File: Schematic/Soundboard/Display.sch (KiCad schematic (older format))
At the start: 2 parts, among them J5 Conn_01x40_MountingPin

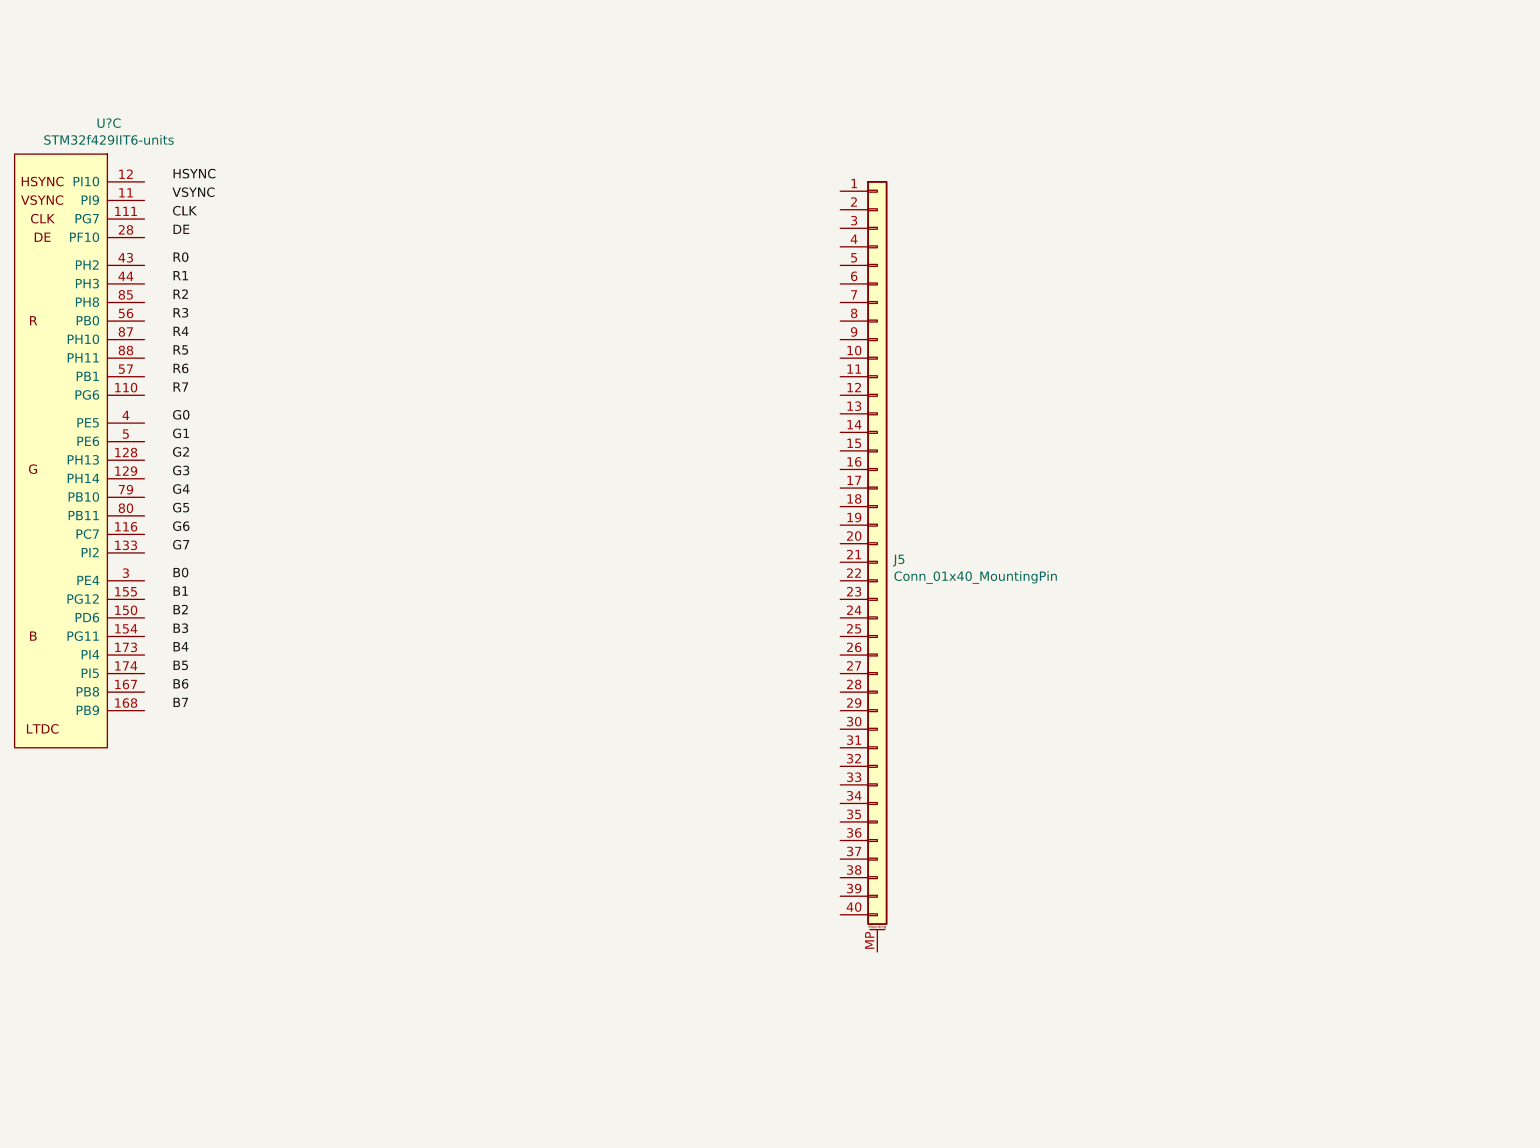
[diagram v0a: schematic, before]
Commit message: Complete part selection. Start connections
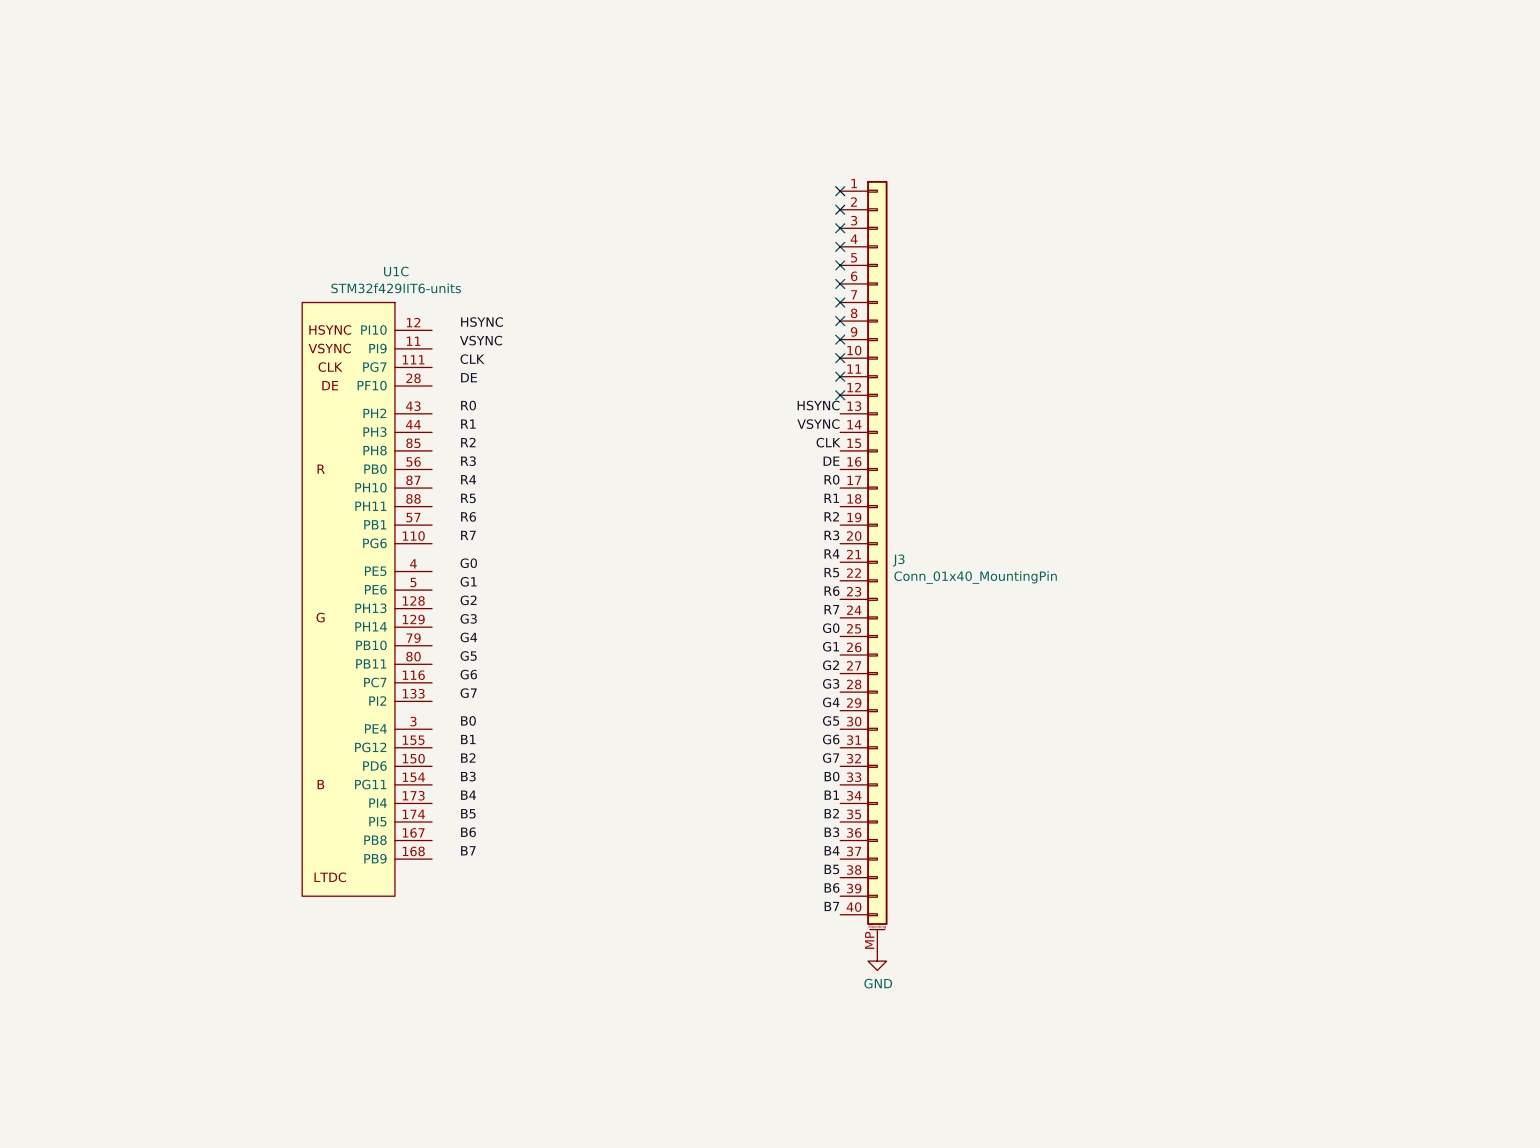
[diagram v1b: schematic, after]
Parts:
- removed U?: STM32f429IIT6-units, symbol Soundboard:STM32f429IIT6-units
- added U1: STM32f429IIT6-units, symbol Soundboard:STM32f429IIT6-units
- renumbered J5 to J3
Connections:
- net B0: now also J3.33 (Pin_33)
- net B1: now also J3.34 (Pin_34)
- net B2: now also J3.35 (Pin_35)
- net B3: now also J3.36 (Pin_36)
- net B4: now also J3.37 (Pin_37)
- net B5: now also J3.38 (Pin_38)
- net B6: now also J3.39 (Pin_39)
- net B7: now also J3.40 (Pin_40)
- net CLK: now also J3.15 (Pin_15)
- net DE: now also J3.16 (Pin_16)
- net G0: now also J3.25 (Pin_25)
- net G1: now also J3.26 (Pin_26)
- net G2: now also J3.27 (Pin_27)
- net G3: now also J3.28 (Pin_28)
- net G4: now also J3.29 (Pin_29)
- net G5: now also J3.30 (Pin_30)
- net G6: now also J3.31 (Pin_31)
- net G7: now also J3.32 (Pin_32)
- net HSYNC: now also J3.13 (Pin_13)
- net R0: now also J3.17 (Pin_17)
- net R1: now also J3.18 (Pin_18)
- net R2: now also J3.19 (Pin_19)
- net R3: now also J3.20 (Pin_20)
- net R4: now also J3.21 (Pin_21)
- net R5: now also J3.22 (Pin_22)
- net R6: now also J3.23 (Pin_23)
- net R7: now also J3.24 (Pin_24)
- net VSYNC: now also J3.14 (Pin_14)
- net GND: now reaches J3.MP (MountPin)
- no-connect marks 0 -> 12
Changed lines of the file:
@@
 EESchema Schematic File Version 4
-EELAYER 30 0
+LIBS:Soundboard-cache
+EELAYER 26 0
 EELAYER END
 $Descr A4 11693 8268
 encoding utf-8
-Sheet 6 6
+Sheet 5 7
 Title ""
 Date ""
@@
 Comment4 ""
 $EndDescr
-Text Label 3650 1800 0    50   ~ 0
+Text Label 5200 2600 0    50   ~ 0
 HSYNC
-Text Label 3650 1900 0    50   ~ 0
+Text Label 5200 2700 0    50   ~ 0
 VSYNC
-Text Label 3650 3800 0    50   ~ 0
+Text Label 5200 4600 0    50   ~ 0
 G7
-Text Label 3650 3700 0    50   ~ 0
+Text Label 5200 4500 0    50   ~ 0
 G6
-Text Label 3650 3600 0    50   ~ 0
+Text Label 5200 4400 0    50   ~ 0
 G5
-Text Label 3650 3100 0    50   ~ 0
+Text Label 5200 3900 0    50   ~ 0
 G0
-Text Label 3650 3200 0    50   ~ 0
+Text Label 5200 4000 0    50   ~ 0
 G1
-Text Label 3650 3500 0    50   ~ 0
+Text Label 5200 4300 0    50   ~ 0
 G4
-Text Label 3650 3400 0    50   ~ 0
+Text Label 5200 4200 0    50   ~ 0
 G3
-Text Label 3650 3300 0    50   ~ 0
+Text Label 5200 4100 0    50   ~ 0
 G2
-Text Label 3650 2650 0    50   ~ 0
+Text Label 5200 3450 0    50   ~ 0
 R4
-Text Label 3650 2450 0    50   ~ 0
+Text Label 5200 3250 0    50   ~ 0
 R2
-Text Label 3650 2350 0    50   ~ 0
+Text Label 5200 3150 0    50   ~ 0
 R1
-Text Label 3650 2250 0    50   ~ 0
+Text Label 5200 3050 0    50   ~ 0
 R0
-Text Label 3650 2000 0    50   ~ 0
+Text Label 5200 2800 0    50   ~ 0
 CLK
-Text Label 3650 2950 0    50   ~ 0
+Text Label 5200 3750 0    50   ~ 0
 R7
-Text Label 3650 2100 0    50   ~ 0
+Text Label 5200 2900 0    50   ~ 0
 DE
-Text Label 3650 2550 0    50   ~ 0
+Text Label 5200 3350 0    50   ~ 0
 R3
-Text Label 3650 2850 0    50   ~ 0
+Text Label 5200 3650 0    50   ~ 0
 R6
-Text Label 3650 2750 0    50   ~ 0
+Text Label 5200 3550 0    50   ~ 0
 R5
-Text Label 3650 4150 0    50   ~ 0
+Text Label 5200 4950 0    50   ~ 0
 B2
-Text Label 3650 4450 0    50   ~ 0
+Text Label 5200 5250 0    50   ~ 0
 B5
-Text Label 3650 4650 0    50   ~ 0
+Text Label 5200 5450 0    50   ~ 0
 B7
-Text Label 3650 4550 0    50   ~ 0
+Text Label 5200 5350 0    50   ~ 0
 B6
-Text Label 3650 4250 0    50   ~ 0
+Text Label 5200 5050 0    50   ~ 0
 B3
-Text Label 3650 4050 0    50   ~ 0
+Text Label 5200 4850 0    50   ~ 0
 B1
-Text Label 3650 3950 0    50   ~ 0
+Text Label 5200 4750 0    50   ~ 0
 B0
-Text Label 3650 4350 0    50   ~ 0
+Text Label 5200 5150 0    50   ~ 0
 B4
 $Comp
-L Connector_Generic_MountingPin:Conn_01x40_MountingPin J5
+L Connector_Generic_MountingPin:Conn_01x40_MountingPin J3
 U 1 1 5F647763
 P 7450 3750
-F 0 "J5" H 7538 3664 50  0000 L CNN
+F 0 "J3" H 7538 3664 50  0000 L CNN
 F 1 "Conn_01x40_MountingPin" H 7538 3573 50  0000 L CNN
 F 2 "Connector_FFC-FPC:TE_4-1734839-0_1x40-1MP_P0.5mm_Horizontal" H 7450 3750 50  0001 C CNN
@@
 $EndComp
 $Comp
-L Soundboard:STM32f429IIT6-units U?
-U 3 1 5F43D80A
-P 3050 1550
-F 0 "U?" H 3308 1615 50  0000 C CNN
-F 1 "STM32f429IIT6-units" H 3308 1524 50  0000 C CNN
-F 2 "" H 3050 1550 50  0001 C CNN
-F 3 "" H 3050 1550 50  0001 C CNN
-	3    3050 1550
+L Soundboard:STM32f429IIT6-units U1
+U 3 1 5F39E369
+P 4600 2350
+F 0 "U1" H 4856 2415 50  0000 C CNN
+F 1 "STM32f429IIT6-units" H 4856 2324 50  0000 C CNN
+F 2 "" H 4600 2350 50  0001 C CNN
+F 3 "" H 4600 2350 50  0001 C CNN
+	3    4600 2350
 	1    0    0    -1
 $EndComp
+Text Label 7250 3050 2    50   ~ 0
+HSYNC
+Text Label 7250 3150 2    50   ~ 0
+VSYNC
+Text Label 7250 4950 2    50   ~ 0
+G7
+Text Label 7250 4850 2    50   ~ 0
+G6
+Text Label 7250 4750 2    50   ~ 0
+G5
+Text Label 7250 4250 2    50   ~ 0
+G0
+Text Label 7250 4350 2    50   ~ 0
+G1
+Text Label 7250 4650 2    50   ~ 0
+G4
+Text Label 7250 4550 2    50   ~ 0
+G3
+Text Label 7250 4450 2    50   ~ 0
+G2
+Text Label 7250 3850 2    50   ~ 0
+R4
+Text Label 7250 3650 2    50   ~ 0
+R2
+Text Label 7250 3550 2    50   ~ 0
+R1
+Text Label 7250 3450 2    50   ~ 0
+R0
+Text Label 7250 3250 2    50   ~ 0
+CLK
+Text Label 7250 4150 2    50   ~ 0
+R7
+Text Label 7250 3350 2    50   ~ 0
+DE
+Text Label 7250 3750 2    50   ~ 0
+R3
+Text Label 7250 4050 2    50   ~ 0
+R6
+Text Label 7250 3950 2    50   ~ 0
+R5
+Text Label 7250 5250 2    50   ~ 0
+B2
+Text Label 7250 5550 2    50   ~ 0
+B5
+Text Label 7250 5750 2    50   ~ 0
+B7
+Text Label 7250 5650 2    50   ~ 0
+B6
+Text Label 7250 5350 2    50   ~ 0
+B3
+Text Label 7250 5150 2    50   ~ 0
+B1
+Text Label 7250 5050 2    50   ~ 0
+B0
+Text Label 7250 5450 2    50   ~ 0
+B4
+$Comp
+L power:GND #PWR0102
+U 1 1 5F5ABADE
+P 7450 5950
+F 0 "#PWR0102" H 7450 5700 50  0001 C CNN
+F 1 "GND" H 7455 5777 50  0000 C CNN
+F 2 "" H 7450 5950 50  0001 C CNN
+F 3 "" H 7450 5950 50  0001 C CNN
+	1    7450 5950
+	1    0    0    -1
+$EndComp
+NoConn ~ 7250 2950
+NoConn ~ 7250 2850
+NoConn ~ 7250 2750
+NoConn ~ 7250 2650
+NoConn ~ 7250 2550
+NoConn ~ 7250 2450
+NoConn ~ 7250 2350
+NoConn ~ 7250 2250
+NoConn ~ 7250 2150
+NoConn ~ 7250 2050
+NoConn ~ 7250 1950
+NoConn ~ 7250 1850
 $EndSCHEMATC

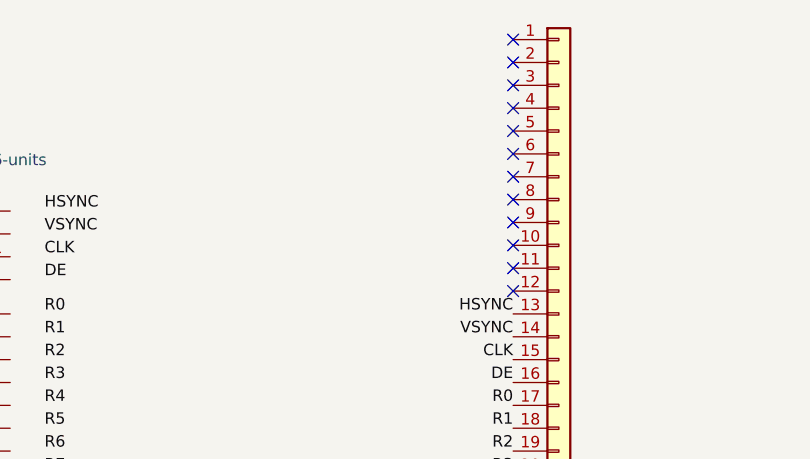
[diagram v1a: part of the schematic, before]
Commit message: Complete connections except for display to be chosen
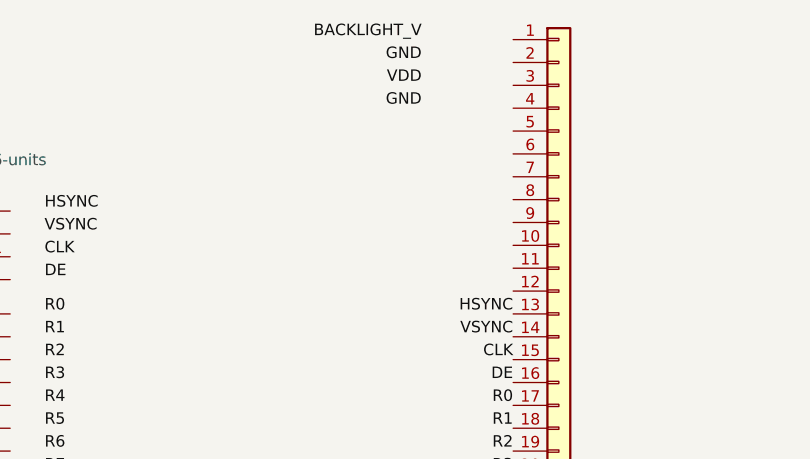
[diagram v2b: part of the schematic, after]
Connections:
- no-connect marks 12 -> 0
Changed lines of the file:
@@
 B4
-$Comp
-L Connector_Generic_MountingPin:Conn_01x40_MountingPin J3
-U 1 1 5F647763
-P 7450 3750
-F 0 "J3" H 7538 3664 50  0000 L CNN
-F 1 "Conn_01x40_MountingPin" H 7538 3573 50  0000 L CNN
-F 2 "Connector_FFC-FPC:TE_4-1734839-0_1x40-1MP_P0.5mm_Horizontal" H 7450 3750 50  0001 C CNN
-F 3 "~" H 7450 3750 50  0001 C CNN
-	1    7450 3750
-	1    0    0    -1
-$EndComp
 $Comp
 L Soundboard:STM32f429IIT6-units U1
@@
 	1    0    0    -1
 $EndComp
-NoConn ~ 7250 2950
-NoConn ~ 7250 2850
-NoConn ~ 7250 2750
-NoConn ~ 7250 2650
-NoConn ~ 7250 2550
-NoConn ~ 7250 2450
-NoConn ~ 7250 2350
-NoConn ~ 7250 2250
-NoConn ~ 7250 2150
-NoConn ~ 7250 2050
-NoConn ~ 7250 1950
-NoConn ~ 7250 1850
+$Comp
+L Connector_Generic_MountingPin:Conn_01x40_MountingPin J3
+U 1 1 5F647763
+P 7450 3750
+F 0 "J3" H 7538 3664 50  0000 L CNN
+F 1 "Conn_01x40_MountingPin" H 7538 3573 50  0000 L CNN
+F 2 "Connector_FFC-FPC:TE_4-1734839-0_1x40-1MP_P0.5mm_Horizontal" H 7450 3750 50  0001 C CNN
+F 3 "~" H 7450 3750 50  0001 C CNN
+	1    7450 3750
+	1    0    0    -1
+$EndComp
+Text Label 6850 2050 2    50   ~ 0
+VDD
+Text Label 6850 2150 2    50   ~ 0
+GND
+Text Label 6850 1850 2    50   ~ 0
+BACKLIGHT_V
+Text Label 6850 1950 2    50   ~ 0
+GND
 $EndSCHEMATC

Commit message: Additional rework
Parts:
- removed J3: Conn_01x40_MountingPin, Connector_FFC-FPC:TE_4-1734839-0_1x40-1MP_P0.5mm_Horizontal, symbol Connector_Generic_MountingPin:Conn_01x40_MountingPin
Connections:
- net B0: now also U1.3 (PE4)
- net B1: now also U1.155 (PG12)
- net B2: now also U1.150 (PD6)
- net B3: now also U1.154 (PG11)
- net B4: now also U1.173 (PI4)
- net B5: now also U1.174 (PI5)
- net B6: now also U1.167 (PB8)
- net B7: now also U1.168 (PB9)
- net CLK: now also U1.111 (PG7)
- net DE: now also U1.28 (PF10)
- net G0: now also U1.4 (PE5)
- net G1: now also U1.5 (PE6)
- net G2: now also U1.128 (PH13)
- net G3: now also U1.129 (PH14)
- net G4: now also U1.79 (PB10)
- net G5: now also U1.80 (PB11)
- net G6: now also U1.116 (PC7)
- net G7: now also U1.133 (PI2)
- net HSYNC: now also U1.12 (PI10)
- net R0: now also U1.43 (PH2)
- net R1: now also U1.44 (PH3)
- net R2: now also U1.85 (PH8)
- net R3: now also U1.56 (PB0)
- net R4: now also U1.87 (PH10)
- net R5: now also U1.88 (PH11)
- net R6: now also U1.57 (PB1)
- net R7: now also U1.110 (PG6)
- net VSYNC: now also U1.11 (PI9)
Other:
- moved on the sheet: U1C
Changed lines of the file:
@@
 EESchema Schematic File Version 4
-LIBS:Soundboard-cache
-EELAYER 26 0
+EELAYER 30 0
 EELAYER END
 $Descr A4 11693 8268
@@
 L Soundboard:STM32f429IIT6-units U1
 U 3 1 5F39E369
-P 4600 2350
-F 0 "U1" H 4856 2415 50  0000 C CNN
-F 1 "STM32f429IIT6-units" H 4856 2324 50  0000 C CNN
-F 2 "" H 4600 2350 50  0001 C CNN
-F 3 "" H 4600 2350 50  0001 C CNN
-	3    4600 2350
+P 4750 2350
+F 0 "U1" H 5006 2415 50  0000 C CNN
+F 1 "STM32f429IIT6-units" H 5006 2324 50  0000 C CNN
+F 2 "" H 4750 2350 50  0001 C CNN
+F 3 "" H 4750 2350 50  0001 C CNN
+	3    4750 2350
 	1    0    0    -1
 $EndComp
-Text Label 7250 3050 2    50   ~ 0
-HSYNC
-Text Label 7250 3150 2    50   ~ 0
-VSYNC
-Text Label 7250 4950 2    50   ~ 0
-G7
-Text Label 7250 4850 2    50   ~ 0
-G6
-Text Label 7250 4750 2    50   ~ 0
-G5
-Text Label 7250 4250 2    50   ~ 0
-G0
-Text Label 7250 4350 2    50   ~ 0
-G1
-Text Label 7250 4650 2    50   ~ 0
-G4
-Text Label 7250 4550 2    50   ~ 0
-G3
-Text Label 7250 4450 2    50   ~ 0
-G2
-Text Label 7250 3850 2    50   ~ 0
-R4
-Text Label 7250 3650 2    50   ~ 0
-R2
-Text Label 7250 3550 2    50   ~ 0
-R1
-Text Label 7250 3450 2    50   ~ 0
-R0
-Text Label 7250 3250 2    50   ~ 0
-CLK
-Text Label 7250 4150 2    50   ~ 0
-R7
-Text Label 7250 3350 2    50   ~ 0
-DE
-Text Label 7250 3750 2    50   ~ 0
-R3
-Text Label 7250 4050 2    50   ~ 0
-R6
-Text Label 7250 3950 2    50   ~ 0
-R5
-Text Label 7250 5250 2    50   ~ 0
-B2
-Text Label 7250 5550 2    50   ~ 0
-B5
-Text Label 7250 5750 2    50   ~ 0
-B7
-Text Label 7250 5650 2    50   ~ 0
-B6
-Text Label 7250 5350 2    50   ~ 0
-B3
-Text Label 7250 5150 2    50   ~ 0
-B1
-Text Label 7250 5050 2    50   ~ 0
-B0
-Text Label 7250 5450 2    50   ~ 0
-B4
-$Comp
-L power:GND #PWR0102
-U 1 1 5F5ABADE
-P 7450 5950
-F 0 "#PWR0102" H 7450 5700 50  0001 C CNN
-F 1 "GND" H 7455 5777 50  0000 C CNN
-F 2 "" H 7450 5950 50  0001 C CNN
-F 3 "" H 7450 5950 50  0001 C CNN
-	1    7450 5950
-	1    0    0    -1
-$EndComp
-$Comp
-L Connector_Generic_MountingPin:Conn_01x40_MountingPin J3
-U 1 1 5F647763
-P 7450 3750
-F 0 "J3" H 7538 3664 50  0000 L CNN
-F 1 "Conn_01x40_MountingPin" H 7538 3573 50  0000 L CNN
-F 2 "Connector_FFC-FPC:TE_4-1734839-0_1x40-1MP_P0.5mm_Horizontal" H 7450 3750 50  0001 C CNN
-F 3 "~" H 7450 3750 50  0001 C CNN
-	1    7450 3750
-	1    0    0    -1
-$EndComp
-Text Label 6850 2050 2    50   ~ 0
-VDD
-Text Label 6850 2150 2    50   ~ 0
-GND
-Text Label 6850 1850 2    50   ~ 0
-BACKLIGHT_V
-Text Label 6850 1950 2    50   ~ 0
-GND
 $EndSCHEMATC
